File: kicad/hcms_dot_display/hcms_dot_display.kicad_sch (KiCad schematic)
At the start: 38 parts

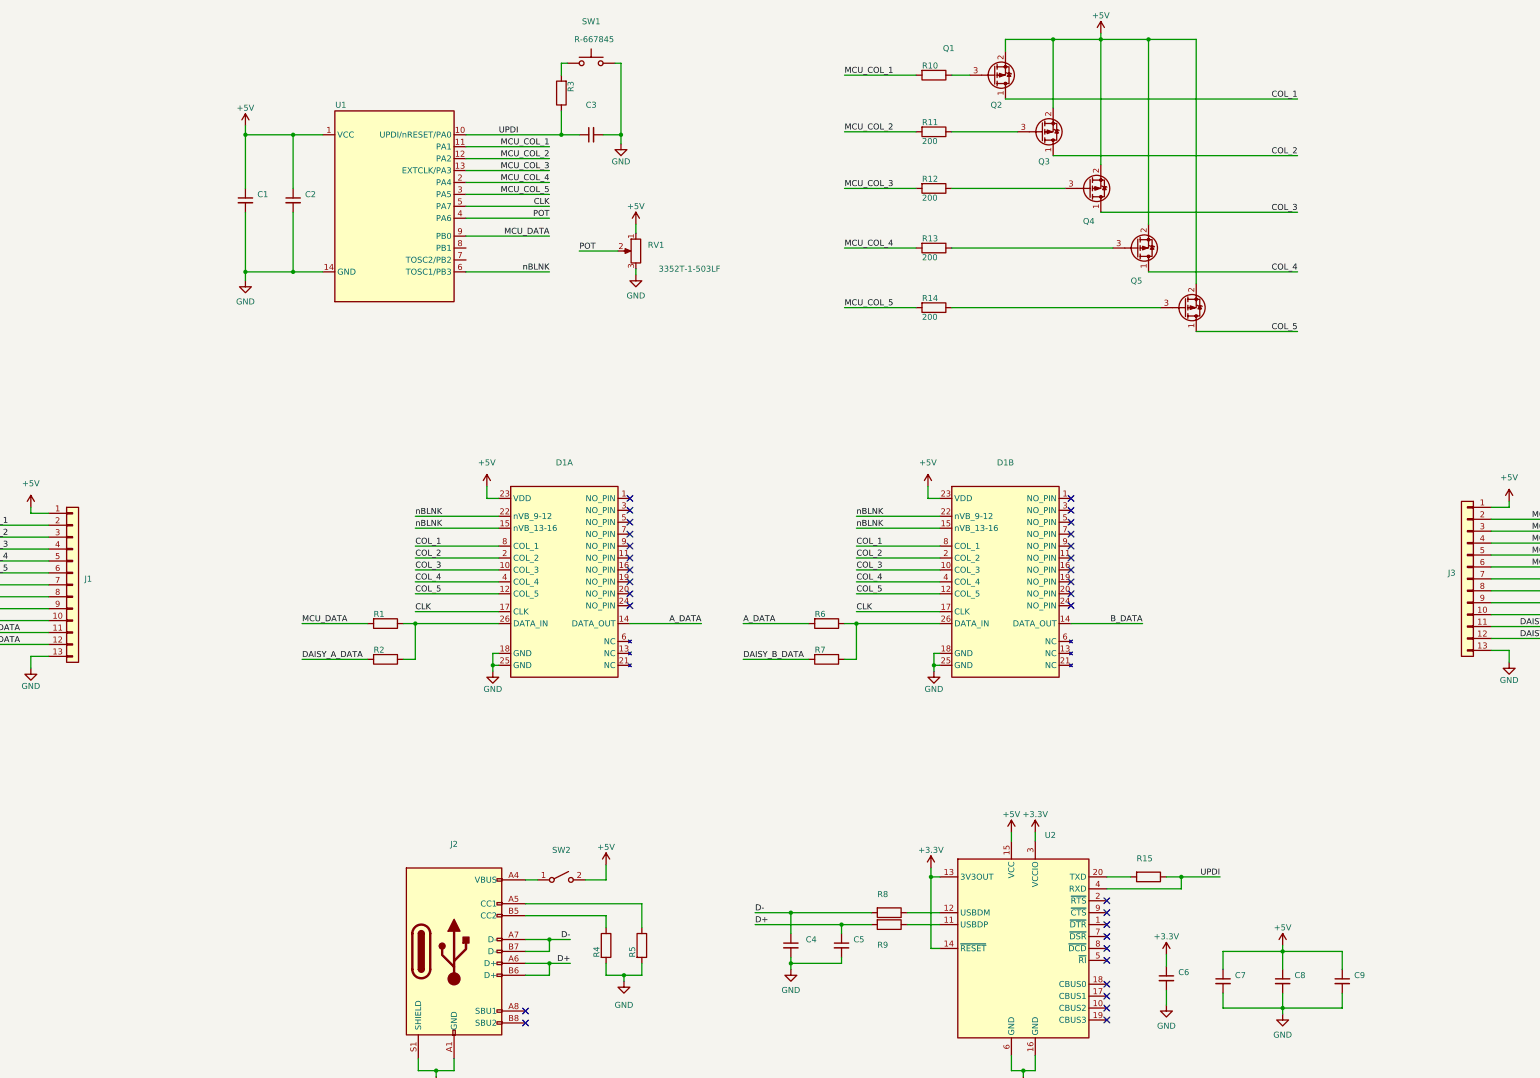
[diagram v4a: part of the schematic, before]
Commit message: slight mods to UPDI circuits
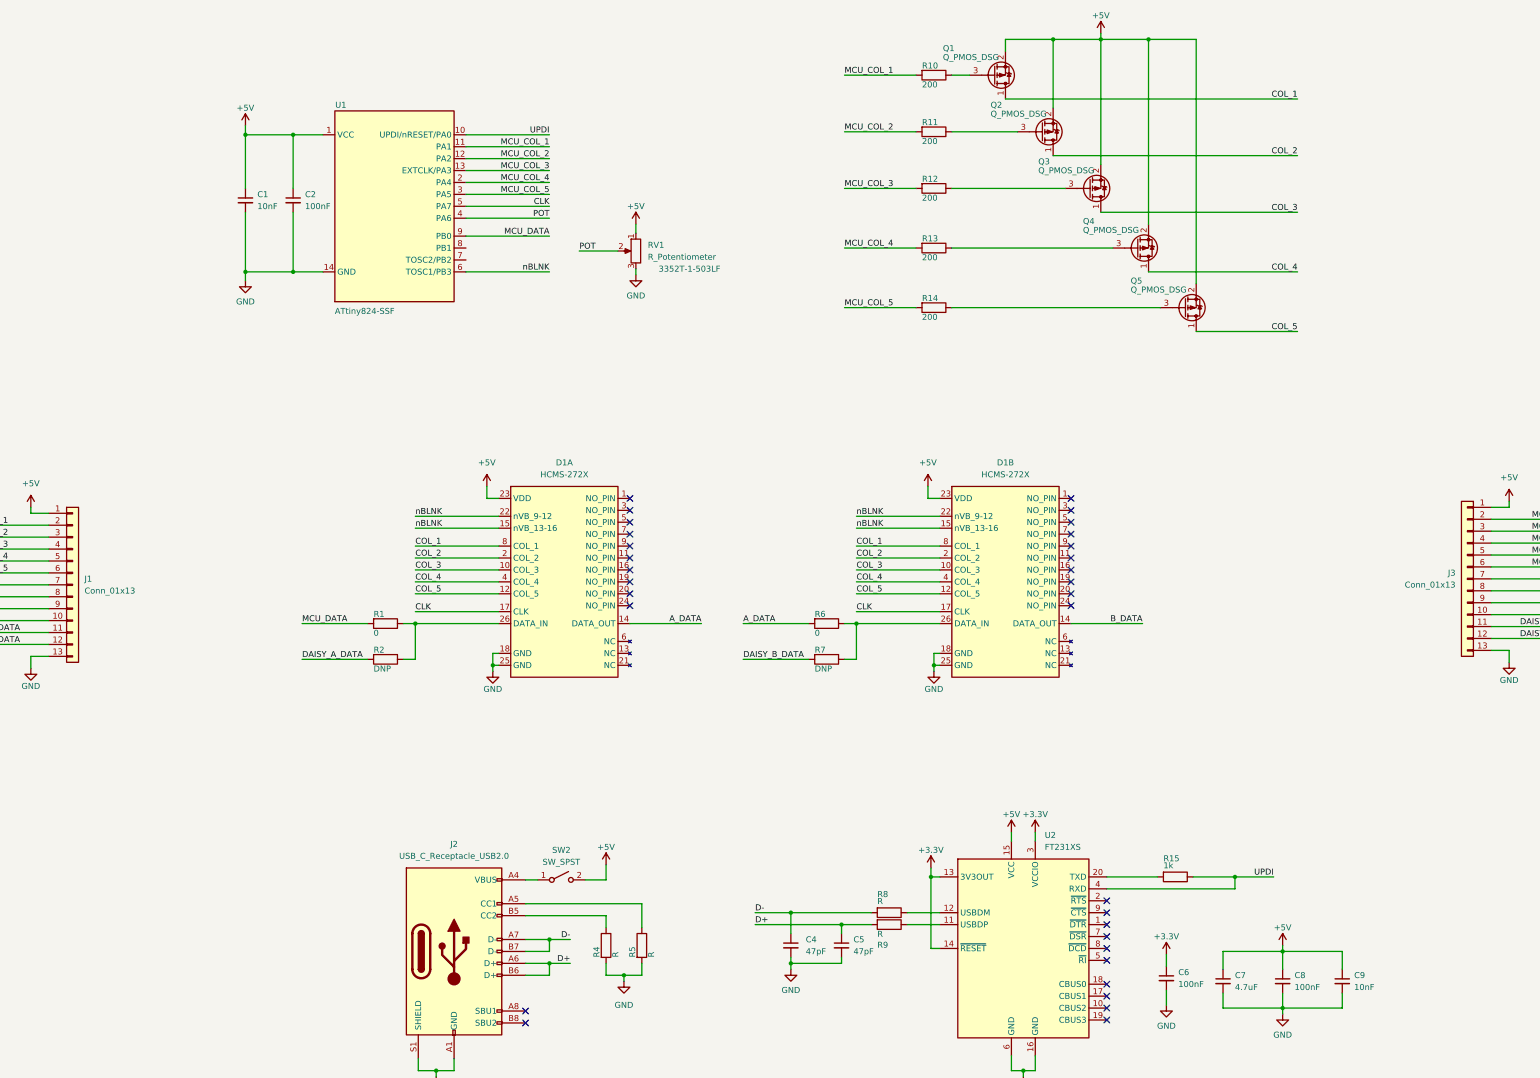
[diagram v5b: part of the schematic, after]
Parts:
- removed C3: (no value), symbol Device:C_Small
- removed R3: (no value), symbol Device:R
- removed SW1: (no value), symbol Switch:SW_Push
- C1, C9: value (none) -> 10nF; footprint (none) -> Capacitor_SMD:C_0603_1608Metric
- C2, C6, C8: value (none) -> 100nF; footprint (none) -> Capacitor_SMD:C_0603_1608Metric
- C4, C5: value (none) -> 47pF; footprint (none) -> Capacitor_SMD:C_0603_1608Metric
- C7: value (none) -> 4.7uF; footprint (none) -> Capacitor_SMD:C_0603_1608Metric
- D1: value (none) -> HCMS-272X; footprint (none) -> hcms:HCMS-2722
- J1, J3: value (none) -> Conn_01x13; footprint (none) -> hcms:board to board con
- J2: value (none) -> USB_C_Receptacle_USB2.0; footprint (none) -> Connector_USB:USB_C_Plug_Molex_105444
- Q1, Q2, Q3, Q4, Q5: value (none) -> Q_PMOS_DSG; footprint (none) -> Package_TO_SOT_SMD:SOT-23
- R1, R6: value (none) -> 0; footprint (none) -> Resistor_SMD:R_0603_1608Metric
- R10: value (none) -> 200; footprint (none) -> Resistor_SMD:R_0603_1608Metric
- R15: value (none) -> 1k; footprint (none) -> Resistor_SMD:R_0603_1608Metric
- R2, R7: value (none) -> DNP; footprint (none) -> Resistor_SMD:R_0603_1608Metric
- R4, R5, R8, R9: value (none) -> R; footprint (none) -> Resistor_SMD:R_0603_1608Metric
- RV1: value (none) -> R_Potentiometer; footprint (none) -> hcms:3352T-1-503LF
- SW2: value (none) -> SW_SPST
- U1: value (none) -> ATtiny824-SSF; footprint (none) -> Package_SO:SOIC-14_3.9x8.7mm_P1.27mm
- U2: value (none) -> FT231XS; footprint (none) -> Package_SO:SSOP-20_3.9x8.7mm_P0.635mm
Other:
- moved on the sheet: R15

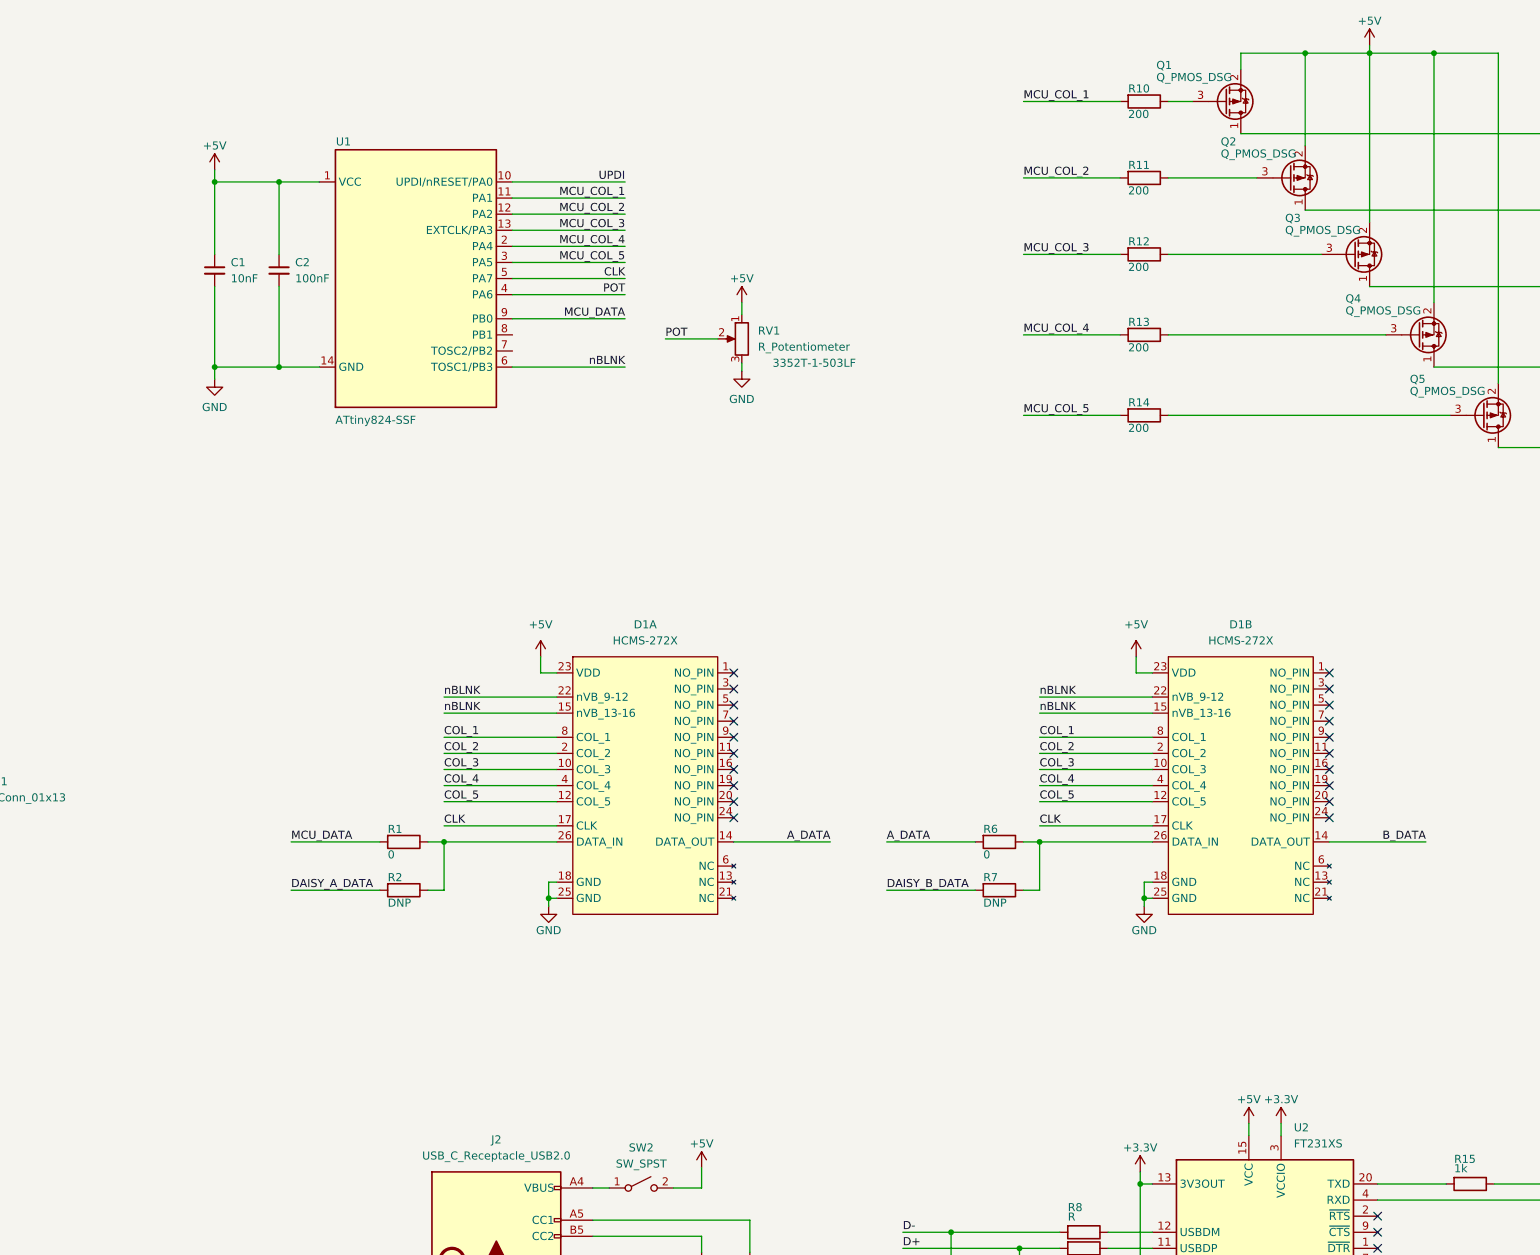
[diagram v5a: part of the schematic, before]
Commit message: Updated dot matrix footprint, experimented with stacked control board design
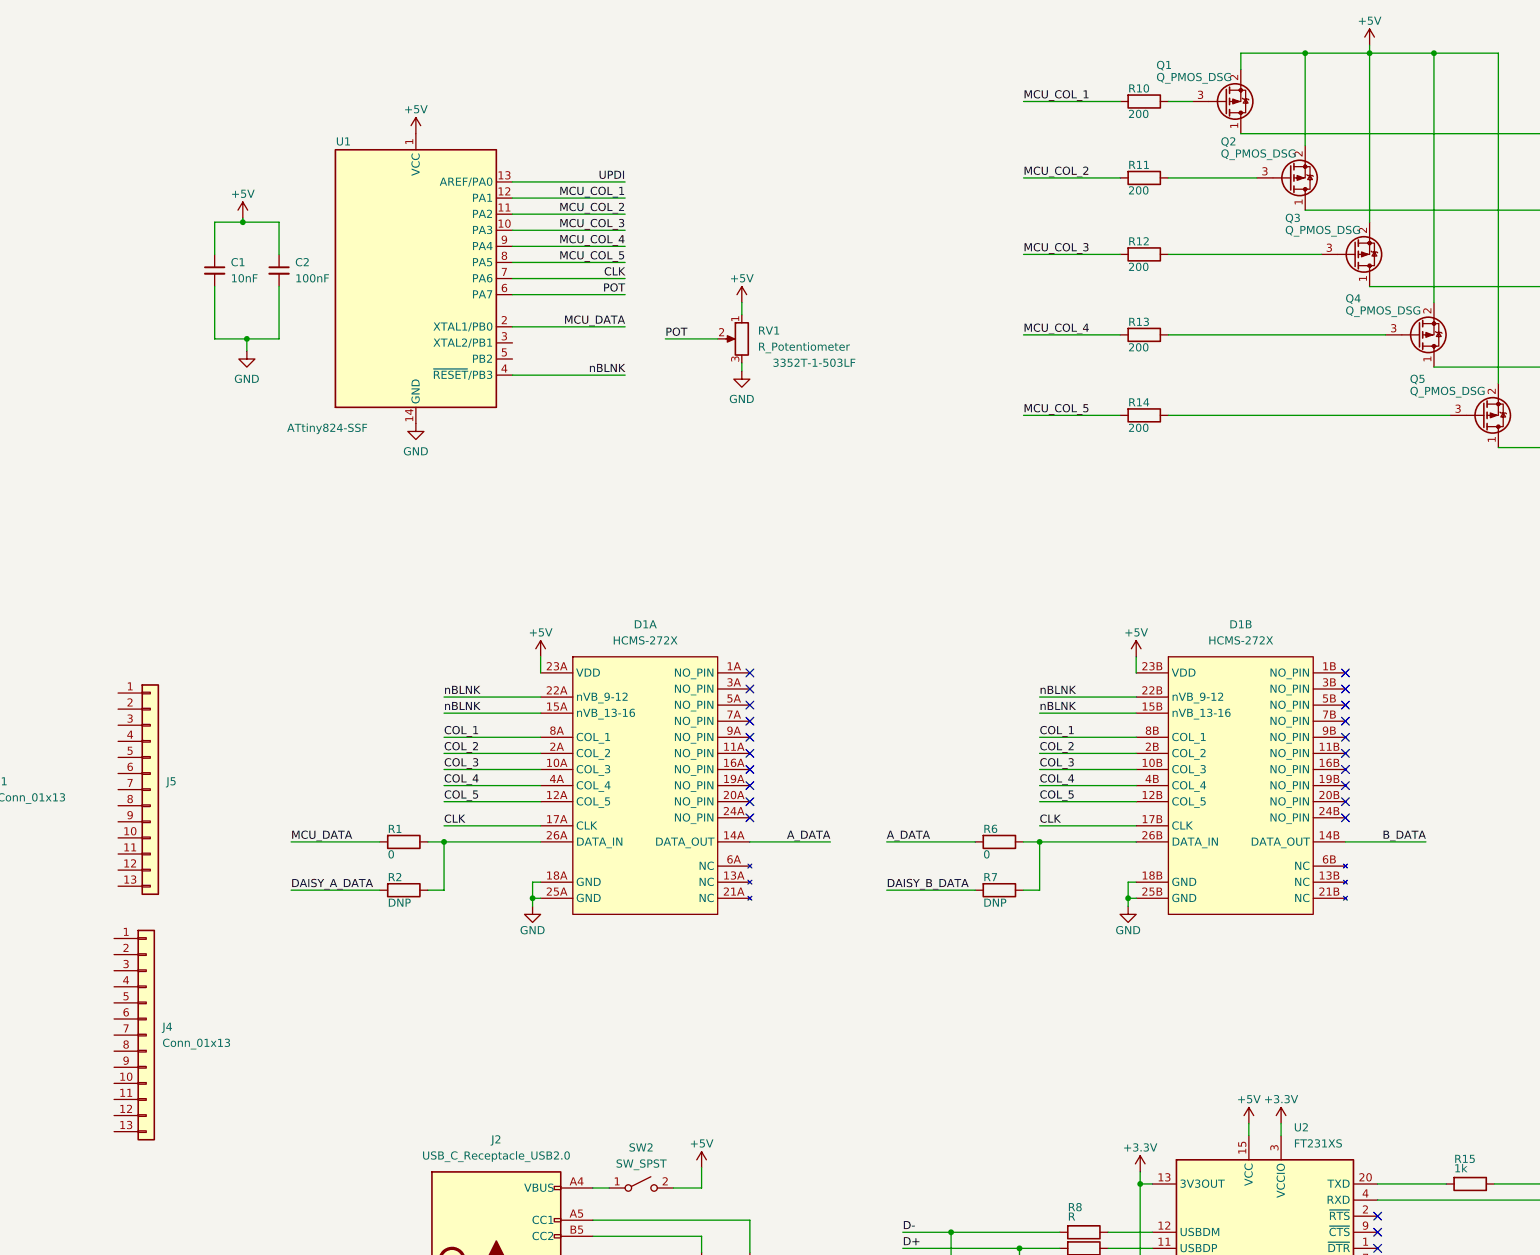
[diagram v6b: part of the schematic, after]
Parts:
- added J4: Conn_01x13, Connector_PinHeader_2.54mm:PinHeader_1x10_P2.54mm_Vertical, symbol Connector_Generic:Conn_01x13
- added J5: (no value), symbol Connector_Generic:Conn_01x13
- C1, C2, C4, C5, C6, C7, C8, C9: footprint Capacitor_SMD:C_0603_1608Metric -> (none)
- R1, R10, R11, R12, R13, R14, R15, R2, R4, R5, R6, R7, R8, R9: footprint Resistor_SMD:R_0603_1608Metric -> (none)
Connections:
- net +5V: now also D1.23A (VDD), D1.23B (VDD); no longer D1.23 (VDD), D1.23 (VDD)
- net A_DATA: now also D1.14A (DATA_OUT); no longer D1.14 (DATA_OUT)
- net B_DATA: now also D1.14B (DATA_OUT); no longer D1.14 (DATA_OUT)
- net CLK: now also D1.17A (CLK), D1.17B (CLK), U1.7 (PA6); no longer D1.17 (CLK), D1.17 (CLK), U1.5 (PA7)
- net COL_1: now also D1.8A (COL_1), D1.8B (COL_1); no longer D1.8 (COL_1), D1.8 (COL_1)
- net COL_2: now also D1.2A (COL_2), D1.2B (COL_2); no longer D1.2 (COL_2), D1.2 (COL_2)
- net COL_3: now also D1.10A (COL_3), D1.10B (COL_3); no longer D1.10 (COL_3), D1.10 (COL_3)
- net COL_4: now also D1.4A (COL_4), D1.4B (COL_4); no longer D1.4 (COL_4), D1.4 (COL_4)
- net COL_5: now also D1.12A (COL_5), D1.12B (COL_5); no longer D1.12 (COL_5), D1.12 (COL_5)
- net GND: now also D1.18A (GND), D1.18B (GND), D1.25A (GND), D1.25B (GND); no longer D1.18 (GND), D1.18 (GND), D1.25 (GND), D1.25 (GND)
- net MCU_COL_1: now also U1.12 (PA1); no longer U1.11 (PA1)
- net MCU_COL_2: now also U1.11 (PA2); no longer U1.12 (PA2)
- net MCU_COL_3: now also U1.10 (PA3); no longer U1.13 (EXTCLK/PA3)
- net MCU_COL_4: now also U1.9 (PA4); no longer U1.2 (PA4)
- net MCU_COL_5: now also U1.8 (PA5); no longer U1.3 (PA5)
- net MCU_DATA: now also U1.2 (XTAL1/PB0); no longer U1.9 (PB0)
- net POT: now also U1.6 (PA7); no longer U1.4 (PA6)
- net UPDI: now also U1.13 (AREF/PA0); no longer U1.10 (UPDI/nRESET/PA0)
- net nBLNK: now also D1.15A (nVB_13-16), D1.15B (nVB_13-16), D1.22A (nVB_9-12), D1.22B (nVB_9-12), U1.4 (~{RESET}/PB3); no longer D1.15 (nVB_13-16), D1.15 (nVB_13-16), D1.22 (nVB_9-12), D1.22 (nVB_9-12), U1.6 (TOSC1/PB3)
- net at R1.1, R2.1: now also D1.26A (DATA_IN); no longer D1.26 (DATA_IN)
- net at R6.1, R7.1: now also D1.26B (DATA_IN); no longer D1.26 (DATA_IN)
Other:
- moved on the sheet: U1
